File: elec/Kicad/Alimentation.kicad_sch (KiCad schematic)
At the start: 33 parts, among them J7 USB_B_Micro_MAIN, Q1 SI2323DS-T1, Q6 SI2323DS-T1, SW4 SW_ON/OFF, U7 TLV62085RLTR

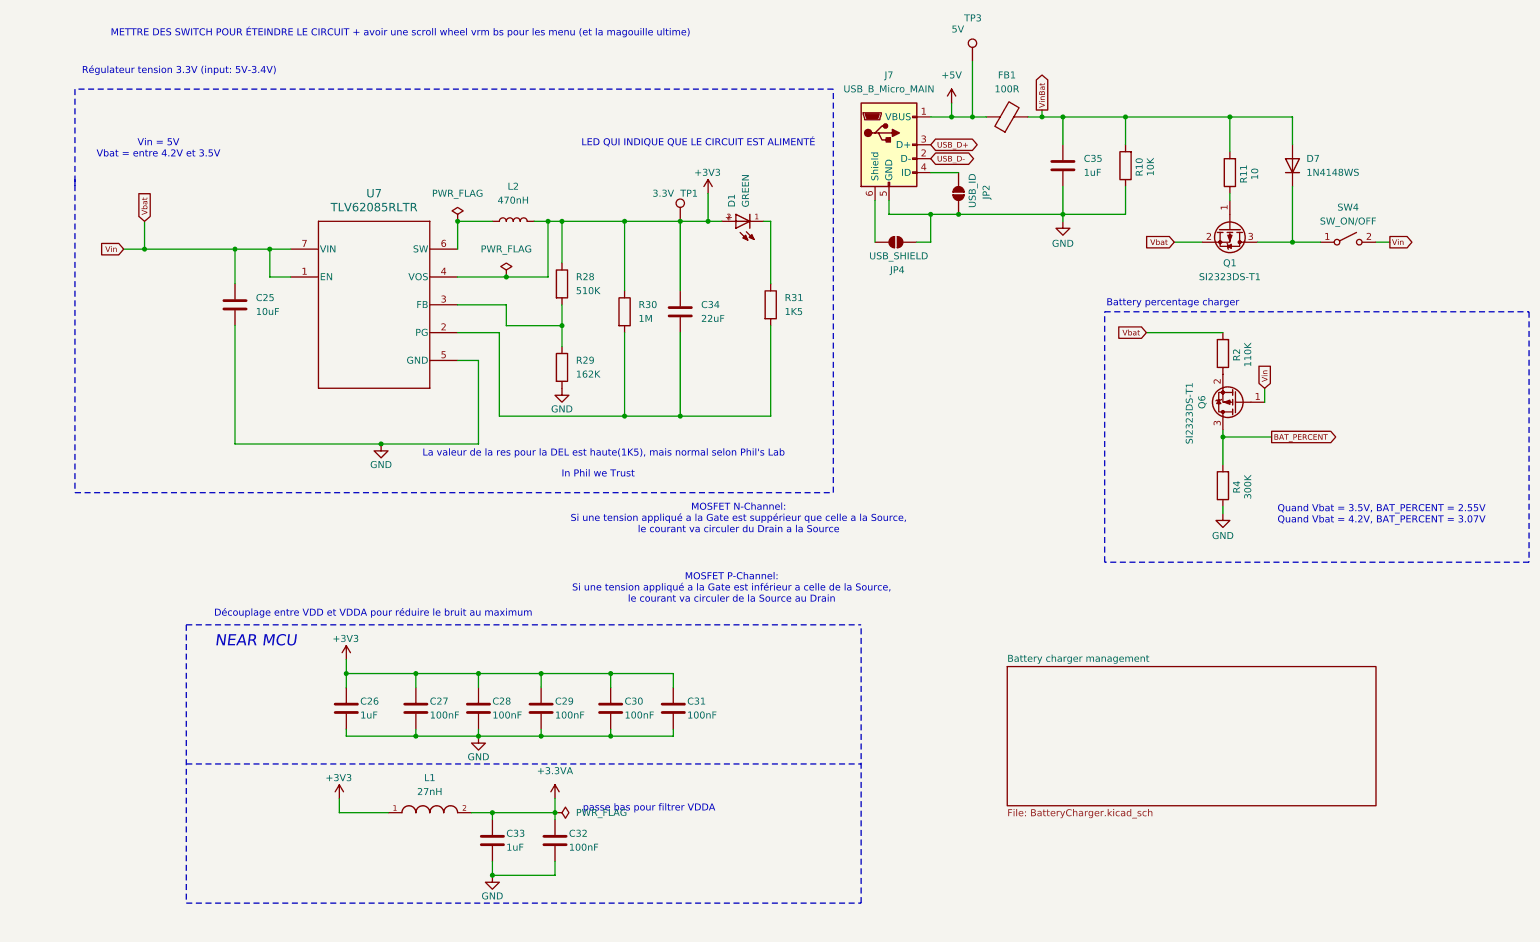
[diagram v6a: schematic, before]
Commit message: ajout d'un Mosfet de type N pour pouvoir gérer le % de batterie (ADC)
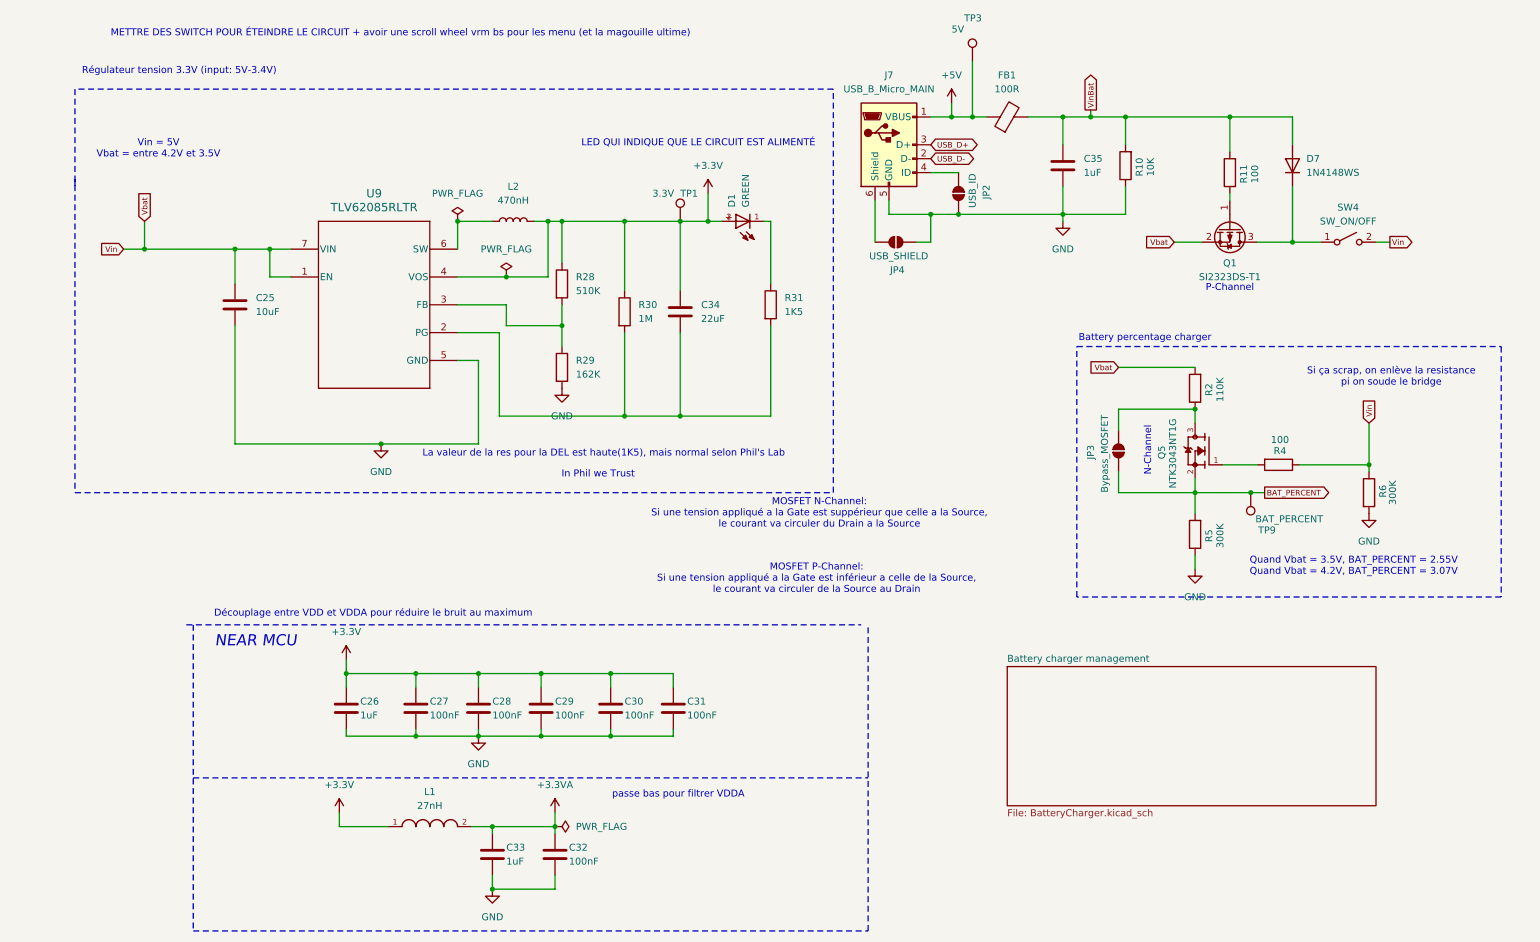
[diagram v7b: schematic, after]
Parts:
- removed Q6: SI2323DS-T1, Package_TO_SOT_SMD:SOT-23, symbol Transistor_FET:AO3401A
- removed U7: TLV62085RLTR, TLV62085RLTR:RLT0007A, symbol TLV62085RLTR:TLV62085RLTR
- added JP3: Bypass_MOSFET, Jumper:SolderJumper-2_P1.3mm_Open_TrianglePad1.0x1.5mm, symbol Jumper:SolderJumper_2_Open
- added Q5: NTK3043NT1G, NTK3043NT1G:SOT40P120X55-3N, symbol NTK3043NT1G:NTK3043NT1G
- added R5, R6: 300K, Resistor_SMD:R_0603_1608Metric_Pad0.98x0.95mm_HandSolder, symbol Device:R
- added TP9: BAT_PERCENT, TestPoint:TestPoint_Loop_D1.80mm_Drill1.0mm_Beaded, symbol Connector:TestPoint
- added U9: TLV62085RLTR, RLT0007A, symbol TLV62085RLTR:TLV62085RLTR
- R11: value 10 -> 100
- R4: value 300K -> 100
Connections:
- net BAT_PERCENT: now also JP3.2 (B), Q5.2, R5.2, TP9.1; no longer R4.2
- net GND: now also R5.1, R6.2, U9.5 (GND); no longer R4.1
- net Vbat: now also R4.1, R6.1, U9.1 (EN), U9.7 (VIN)
- net at R2.1: now also JP3.1 (A), Q5.3
- net at C34.2, R30.2, R31.2: now also U9.2 (PG)
- net at R28.2, R29.1: now also U9.3 (FB)
- net at L2.1: now also U9.6 (SW)
- net +3V3 renamed +3.3V
- net +3.3V: now also U9.4 (VOS)
- new net: Q5.1, R4.2
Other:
- note added: "N-Channel"
- note added: "P-Channel"
- note added: "Si ça scrap, on enlève la resistance pi on soude le bridge"
- moved on the sheet: C32, C33, L1

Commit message: quick push
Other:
- note added: "Si ça scrap, on enlève la resistance + mosfet et on soude le bridge"
- note removed: "Si ça scrap, on enlève la resistance pi on soude le bridge"
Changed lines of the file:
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@@
 		)
 	)
-	(text "Si ça scrap, on enlève la resistance \npi on soude le bridge\n"
+	(text "Si ça scrap, on enlève la resistance + mosfet\net on soude le bridge \n"
 		(exclude_from_sim no)
-		(at 255.524 80.518 0)
+		(at 252.476 80.01 0)
 		(effects
 			(font
